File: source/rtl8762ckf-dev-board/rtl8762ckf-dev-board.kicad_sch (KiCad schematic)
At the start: 28 parts, among them J1 u.FL, J3 Conn_02x05_Odd_Even, J4 Conn_02x05_Odd_Even, J5 Conn_01x18, J6 boot, J7 Conn_01x03, J9 Conn_01x13, U3 ME6211C33M5G-N

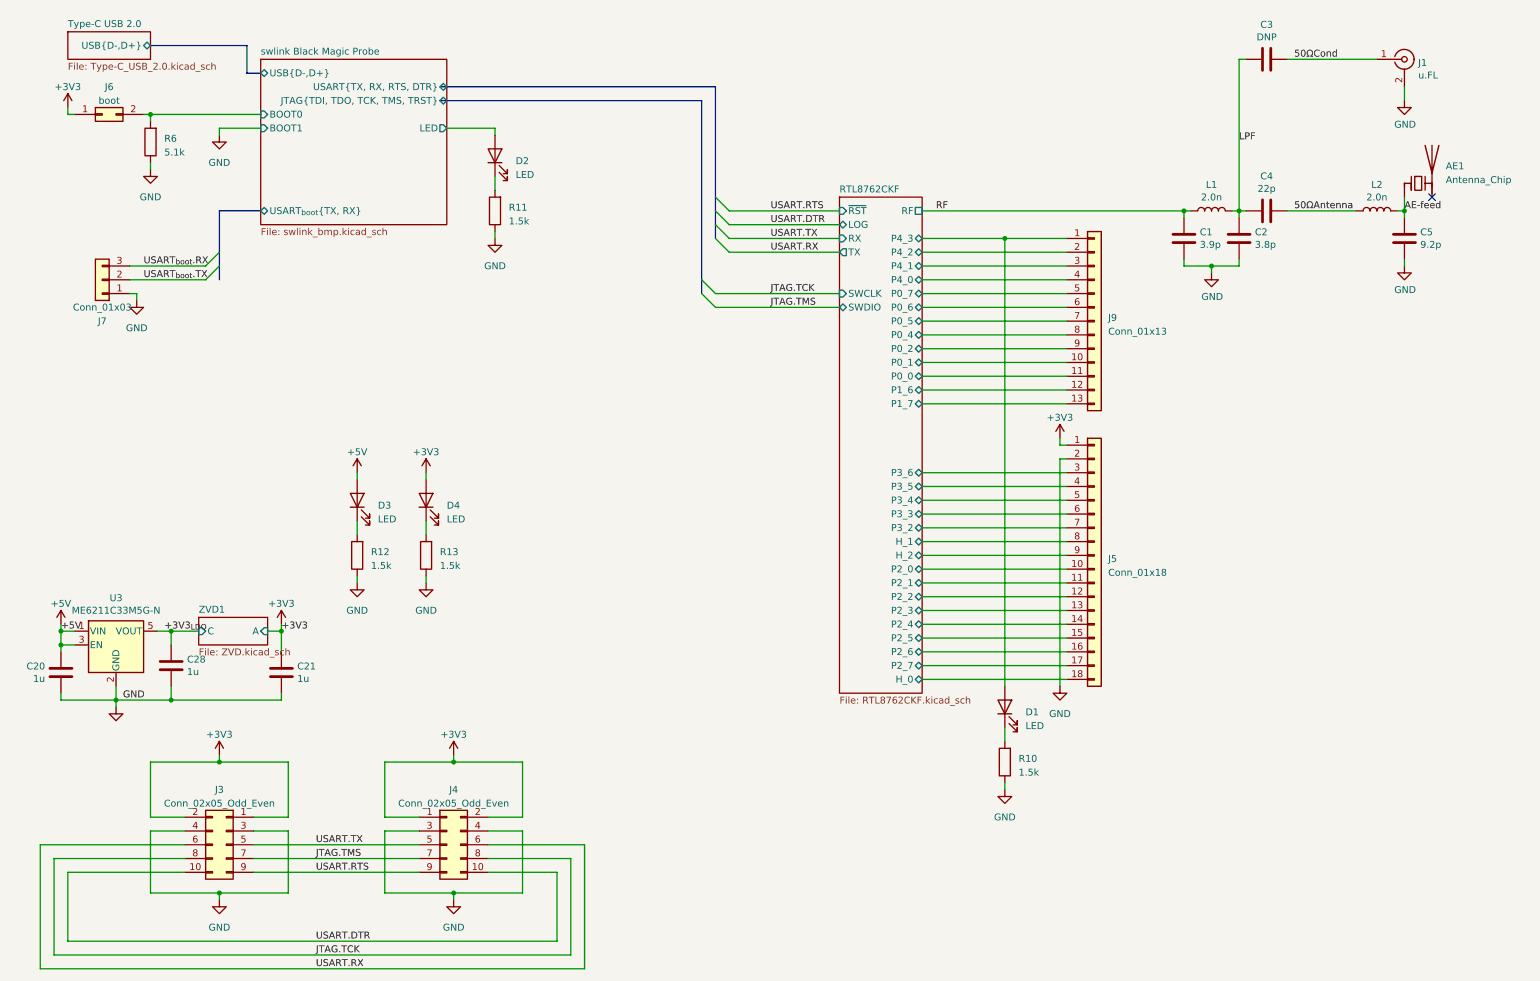
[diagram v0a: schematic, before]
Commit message: implemented pico probe
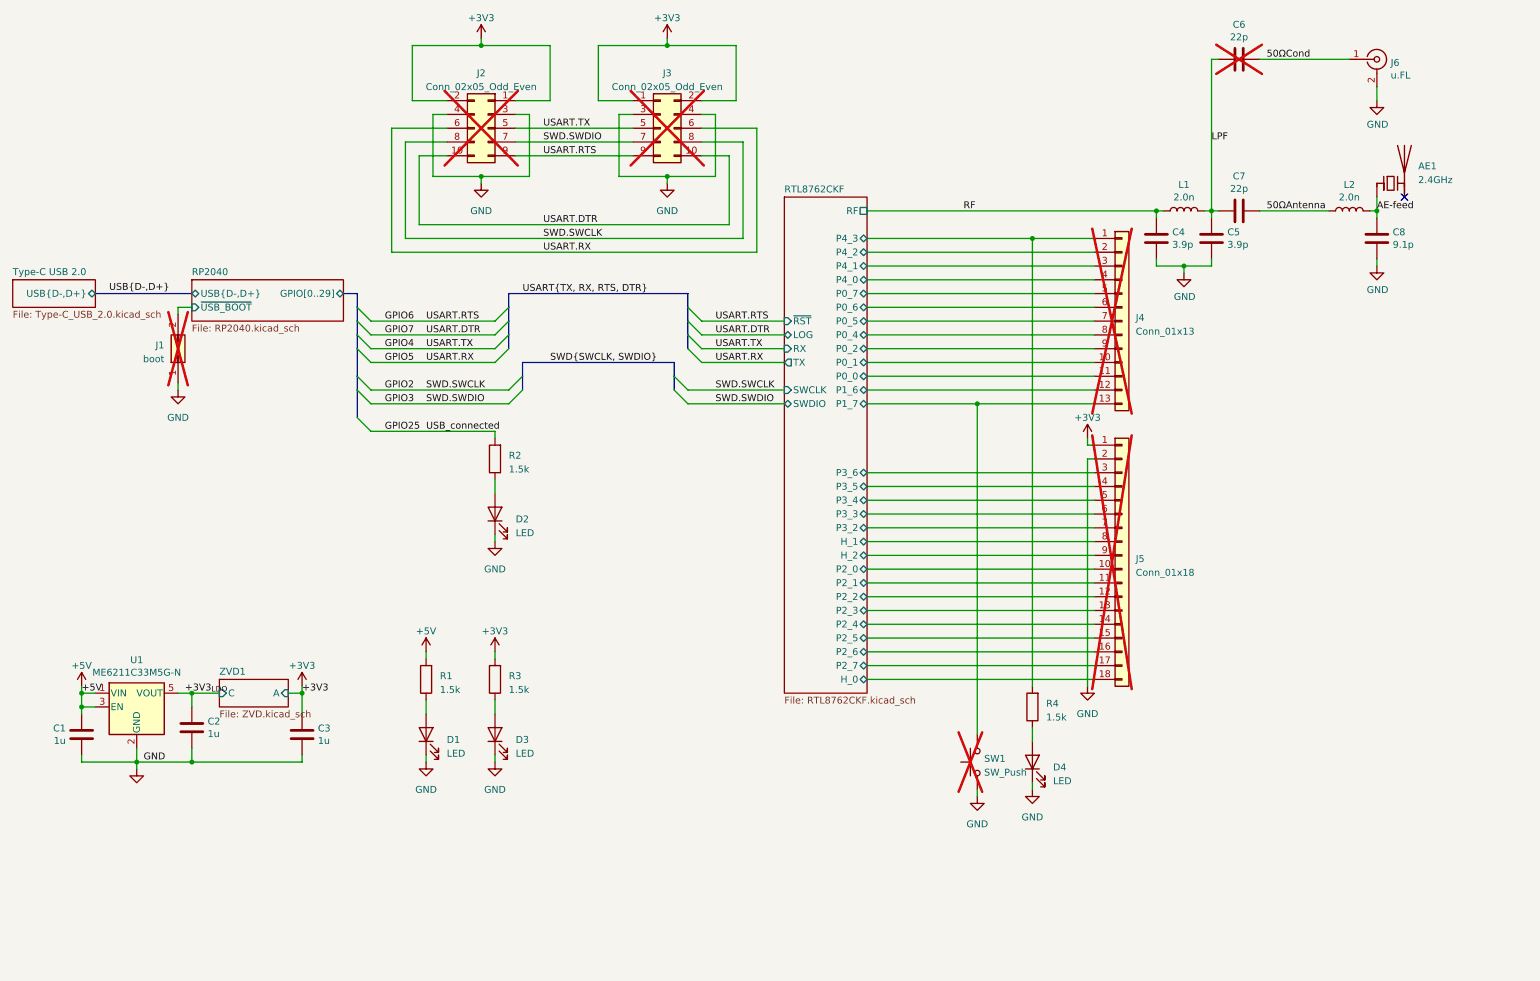
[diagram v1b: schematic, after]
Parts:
- removed J7: Conn_01x03, Connector_PinHeader_2.54mm:PinHeader_1x03_P2.54mm_Vertical, symbol Connector_Generic:Conn_01x03
- removed J9: Conn_01x13, Connector_Castellated:Castellated_1x13_P2.54mm, symbol Connector_Generic:Conn_01x13
- removed R6: 5.1k, Resistor_SMD:R_0402_1005Metric, symbol Device:R
- added J4: Conn_01x13, Connector_PinHeader_2.54mm:PinHeader_1x13_P2.54mm_Vertical, symbol Connector_Generic:Conn_01x13
- added SW1: SW_Push, Button_Switch_SMD:SW_Push_1P1T_NO_6x6mm_H9.5mm, symbol Switch:SW_Push
- AE1: value Antenna_Chip -> 2.4GHz; MPN (none) -> MGMA3216H2450-A02
- C1: renamed from C20; LCSC C5252392 -> C52923; MPN V106M0402X5R100NCT -> CL05A105KA5NQNC
- C2: renamed from C28; LCSC C5252392 -> C52923; MPN V106M0402X5R100NCT -> CL05A105KA5NQNC
- C3: renamed from C21; LCSC C5252392 -> C52923; MPN V106M0402X5R100NCT -> CL05A105KA5NQNC
- C5: renamed from C2; value 3.8p -> 3.9p
- C6: renamed from C3; value DNP -> 22p; LCSC DNP -> C1555; MPN (none) -> 0402CG220J500NT; now not fitted; now left out of the parts list
- C7: renamed from C4; LCSC C295968 -> C1555; MPN (none) -> 0402CG220J500NT
- C8: renamed from C5; value 9.2p -> 9.1p; LCSC C437521 -> C64366
- D1: renamed from D3; footprint LED_SMD:LED_0402_1005Metric -> LED_SMD:LED_0603_1608Metric; LCSC (none) -> C72038; MPN (none) -> 19-213/Y2C-CQ2R2L/3T(CY)
- D2: footprint LED_SMD:LED_0402_1005Metric -> LED_SMD:LED_0603_1608Metric; LCSC (none) -> C72038; MPN (none) -> 19-213/Y2C-CQ2R2L/3T(CY)
- D3: renamed from D4; footprint LED_SMD:LED_0402_1005Metric -> LED_SMD:LED_0603_1608Metric; LCSC (none) -> C72038; MPN (none) -> 19-213/Y2C-CQ2R2L/3T(CY)
- D4: renamed from D1; footprint LED_SMD:LED_0402_1005Metric -> LED_SMD:LED_0603_1608Metric; LCSC (none) -> C72038; MPN (none) -> 19-213/Y2C-CQ2R2L/3T(CY)
- J1: renamed from J6; now not fitted
- J2: renamed from J3; now not fitted
- J3: renamed from J4; now not fitted
- J5: footprint Connector_Castellated:Castellated_1x18_P2.54mm -> Connector_PinHeader_2.54mm:PinHeader_1x18_P2.54mm_Vertical; now not fitted
- J6: renamed from J1; LCSC C88374 -> C5137195; MPN (none) -> BWU.FL-IPEX1
- L1, L2: LCSC C76769 -> C43365; MPN (none) -> SDCL1005C2N0STDF
- R1: renamed from R12; LCSC (none) -> C25867; MPN RC0603FR-071K5L -> 0402WGF1501TCE
- R2: renamed from R11; LCSC (none) -> C25867; MPN RC0603FR-071K5L -> 0402WGF1501TCE
- R3: renamed from R13; LCSC (none) -> C25867; MPN RC0603FR-071K5L -> 0402WGF1501TCE
- R4: renamed from R10; LCSC (none) -> C25867; MPN RC0603FR-071K5L -> 0402WGF1501TCE
- renumbered C1 to C4, U3 to U1
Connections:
- net +3V3: now also R3.2; no longer D3.2 (A), J1.1 (Pin_1)
- net +5V: now also R1.2; no longer D1.2 (A)
- net GND: now also D1.1 (K), D2.1 (K), D3.1 (K), D4.1 (K), J1.1 (Pin_1), SW1.1; no longer R1.1, R2.1, R3.1, R4.1
- net RTL8762CKF/P0_0: now also J4.11 (Pin_11)
- net RTL8762CKF/P0_1: now also J4.10 (Pin_10)
- net RTL8762CKF/P0_2: now also J4.9 (Pin_9)
- net RTL8762CKF/P0_4: now also J4.8 (Pin_8)
- net RTL8762CKF/P0_5: now also J4.7 (Pin_7)
- net RTL8762CKF/P0_6: now also J4.6 (Pin_6)
- net RTL8762CKF/P0_7: now also J4.5 (Pin_5)
- net RTL8762CKF/P1_6: now also J4.12 (Pin_12)
- net RTL8762CKF/P1_7: now also J4.13 (Pin_13), SW1.2
- net RTL8762CKF/P4_0: now also J4.4 (Pin_4)
- net RTL8762CKF/P4_1: now also J4.3 (Pin_3)
- net RTL8762CKF/P4_2: now also J4.2 (Pin_2)
- net RTL8762CKF/P4_3: now also R4.2, J4.1 (Pin_1); no longer D4.2 (A)
- net GPIO25: now reaches R2.2
- net GPIO25: no longer D2.1 (K)
- net JTAG.TCK renamed GPIO2
- net JTAG.TMS renamed GPIO3
- net USART.DTR renamed GPIO7
- net USART.RTS renamed GPIO6
- net USART.RX renamed GPIO5
- net USART.TX renamed GPIO4
- net swlink Black Magic Probe/BOOT0 renamed RP2040/~{USB_BOOT}
- net swlink Black Magic Probe/LED: no longer names the net of D2.2 (A)
- net swlink Black Magic Probe/LED: now also R2.1
- new net: D4.2 (A), R4.1
- new net: D3.2 (A), R3.1
- new net: D1.2 (A), R1.1
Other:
- removed sheet swlink Black Magic Probe
- added sheet RP2040 (RP2040.kicad_sch)
- moved on the sheet: AE1, C1, C2, C3, C4, C5, C7, C8, D1, D2, D3, D4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

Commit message: add net ties to uart lines
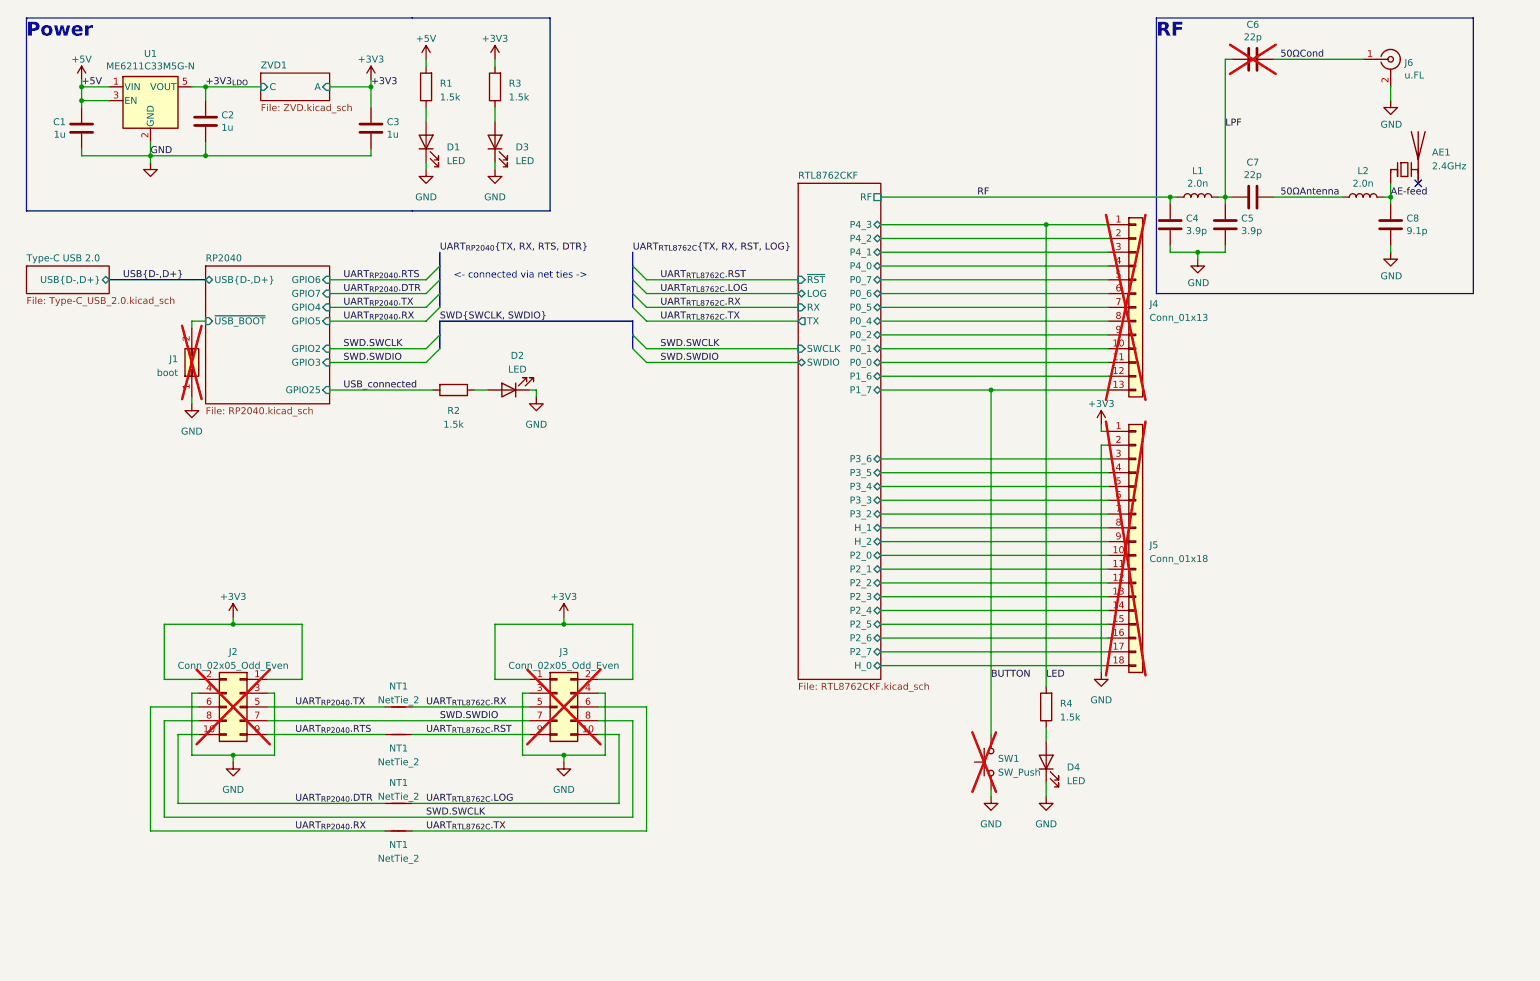
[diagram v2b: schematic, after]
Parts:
- added NT1 (x4): NetTie_2, NetTie_Project:NetTie-2_SMD_Pad0.127mm, symbol Device:NetTie_2
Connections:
- net GPIO2 renamed SWD.SWCLK
- net GPIO25 renamed USB_connected
- net GPIO3 renamed SWD.SWDIO
- net GPIO4 renamed UART_{RP2040}.TX
- net UART_{RP2040}.TX: now also NT1.1; no longer J3.5 (Pin_5)
- net GPIO5 renamed UART_{RP2040}.RX
- net UART_{RP2040}.RX: now also NT1.1; no longer J3.6 (Pin_6)
- net GPIO6 renamed UART_{RP2040}.RTS
- net UART_{RP2040}.RTS: now also NT1.1; no longer J3.9 (Pin_9)
- net GPIO7 renamed UART_{RP2040}.DTR
- net UART_{RP2040}.DTR: now also NT1.1; no longer J3.10 (Pin_10)
- net RTL8762CKF/P1_7 renamed BUTTON
- net RTL8762CKF/P4_3 renamed LED
- new net UART_{RTL8762C}.LOG: J3.10 (Pin_10), NT1.2
- new net UART_{RTL8762C}.RST: J3.9 (Pin_9), NT1.2
- new net UART_{RTL8762C}.RX: J3.5 (Pin_5), NT1.2
- new net UART_{RTL8762C}.TX: J3.6 (Pin_6), NT1.2
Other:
- sheet RP2040 ports: added GPIO2, GPIO25, GPIO3, GPIO4, GPIO5, GPIO6, GPIO7; removed GPIO[0..29]
- note added: "<- connected via net ties ->"
- note added: "Power"
- note added: "RF"
- moved on the sheet: AE1, C1, C2, C3, C4, C5, C6, C7, C8, D1, D2, D3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

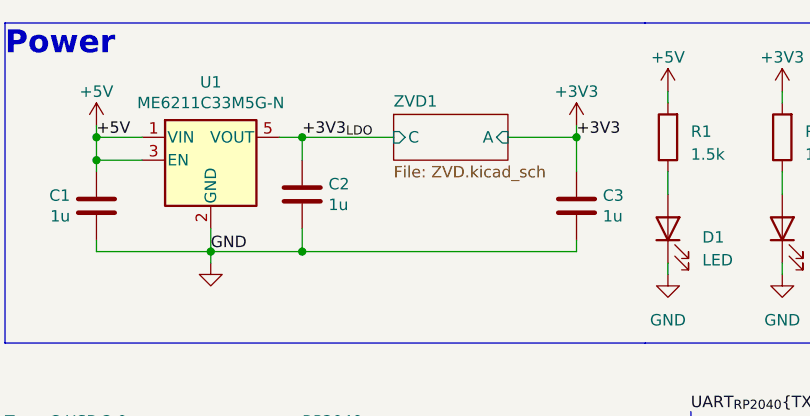
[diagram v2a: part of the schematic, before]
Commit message: correct zvd; closes #4
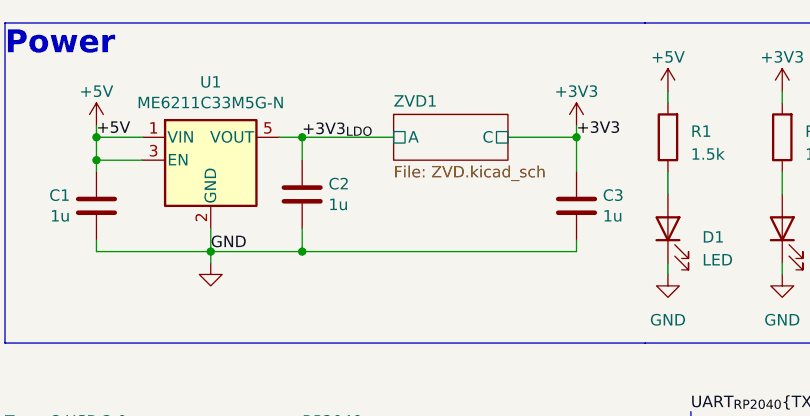
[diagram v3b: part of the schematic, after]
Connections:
- net +3V3_{LDO}: no longer C2.1, U1.5 (VOUT)
- new net ZVD1/A: C2.1, U1.5 (VOUT)
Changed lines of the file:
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@@
+    (stroke (width 0) (type default))
+  )
+  (wire (pts (xy 48.26 27.94) (xy 58.42 27.94))
     (stroke (width 0) (type default))
   )
@@
     (stroke (width 0) (type default))
   )
-  (wire (pts (xy 48.26 27.94) (xy 58.42 27.94))
+  (wire (pts (xy 45.72 27.94) (xy 48.26 27.94))
     (stroke (width 0) (type default))
   )
@@
     (stroke (width 0) (type default))
   )
-  (wire (pts (xy 45.72 27.94) (xy 48.26 27.94))
-    (stroke (width 0) (type default))
-  )
   (polyline (pts (xy 15.24 15.24) (xy 15.24 50.8))
     (stroke (width 0) (type default))
@@
     (effects (font (size 1.27 1.27)) (justify left bottom))
   )
-  (label "UART_{RTL8762C}.TX" (at 132.08 71.12 0)
+  (label "UART_{RTL8762C}.TX" (at 132.08 71.12 0) (fields_autoplaced)
     (effects (font (size 1.27 1.27)) (justify left bottom))
   )
@@
     (effects (font (size 1.27 1.27)) (justify left bottom))
   )
-  (label "UART_{RTL8762C}.LOG" (at 132.08 66.04 0)
+  (label "UART_{RTL8762C}.LOG" (at 132.08 66.04 0) (fields_autoplaced)
     (effects (font (size 1.27 1.27)) (justify left bottom))
   )
@@
     )
   )
-  (label "+3V3_{LDO}" (at 48.26 27.94 0) (fields_autoplaced)
+  (label "+3V3_{LDO}" (at 48.2445 28.0794 0) (fields_autoplaced)
     (effects (font (size 1.27 1.27)) (justify left bottom))
     (property "Netclass" "0.5A" (at 48.26 29.21 0)
@@
     (effects (font (size 1.27 1.27)) (justify left bottom))
   )
-  (label "UART_{RTL8762C}.RST" (at 132.08 63.5 0)
-    (effects (font (size 1.27 1.27)) (justify left bottom))
-  )
-  (label "UART_{RTL8762C}.RX" (at 132.08 68.58 0)
+  (label "UART_{RTL8762C}.RST" (at 132.08 63.5 0) (fields_autoplaced)
+    (effects (font (size 1.27 1.27)) (justify left bottom))
+  )
+  (label "UART_{RTL8762C}.RX" (at 132.08 68.58 0) (fields_autoplaced)
     (effects (font (size 1.27 1.27)) (justify left bottom))
   )
@@
       (effects (font (size 1.27 1.27)) (justify left top))
     )
-    (pin "C" input (at 58.42 27.94 180)
-      (effects (font (size 1.27 1.27)) (justify left))
-    )
-    (pin "A" input (at 71.12 27.94 0)
-      (effects (font (size 1.27 1.27)) (justify right))
-    )
-    (instances
+    (pin "C" passive (at 71.12 27.94 0)
+      (effects (font (size 1.27 1.27)) (justify right))
+    )
+    (pin "A" passive (at 58.42 27.94 180)
+      (effects (font (size 1.27 1.27)) (justify left))
+    )
+    (instances
